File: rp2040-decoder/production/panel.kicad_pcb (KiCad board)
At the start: 4 copper layers, 70 x 70 mm, 535 parts, among them J4 5052702412, Q1 TPM2008, Q2 TPM2008, Q3 TPM2008, Q4 TPM2008, Q5 TPM2008, Q6 TPM2008, Q7 TPM2008, U1 W25Q64JVXGIQ, U2 AP63203WU, U3 RP2040, U4 MD9927, U5 MAX98357A, U6 LMV331, Y1 X252012MMB4SI

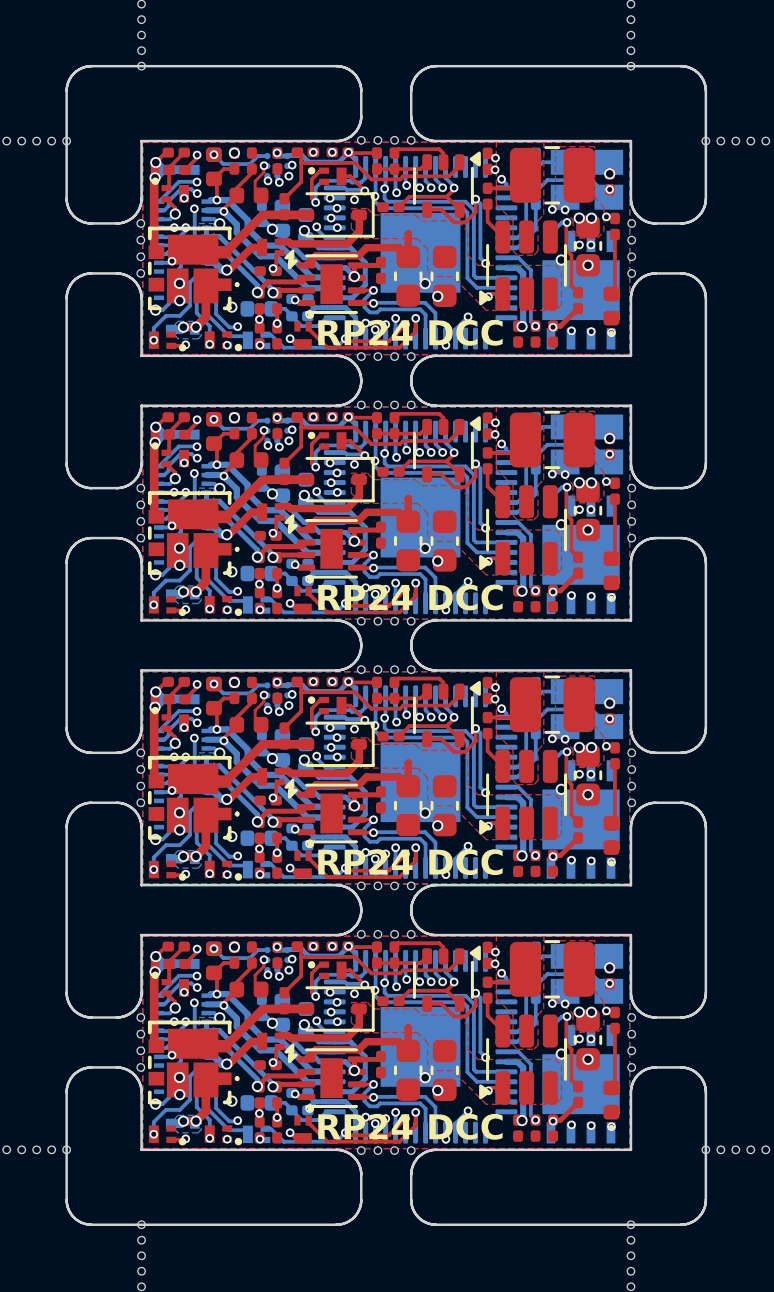
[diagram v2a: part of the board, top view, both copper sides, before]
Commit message: fix: dfm fixes and trace cleanup
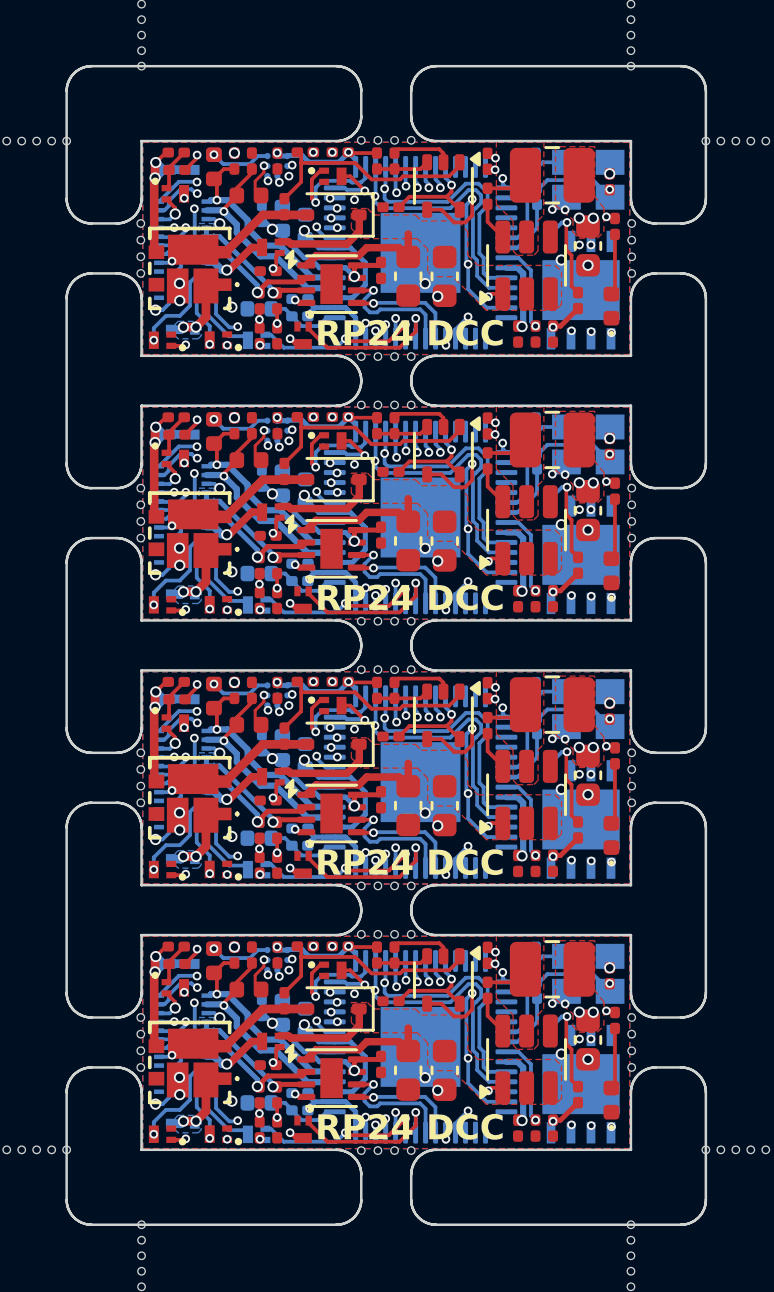
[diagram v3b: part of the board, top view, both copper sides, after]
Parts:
- removed the C8 at (145.3, 38.2)
- removed the C8 at (145.3, 48.8)
- removed the C8 at (145.3, 59.4)
- removed the C8 at (145.3, 70.0)
- removed the R6 at (154.5, 58.2)
- removed the R6 at (154.5, 37.0)
- removed the R6 at (154.5, 47.6)
- removed the R6 at (154.5, 68.8)
- removed the Y1 at (156.5, 36.4)
- removed the Y1 at (156.5, 57.5)
- removed the Y1 at (156.5, 47.0)
- removed the Y1 at (156.5, 68.2)
- added C8: 10uF, Capacitor_SMD:C_0402_1005Metric, B.Cu at (145.3, 38.2)
- added C8: 10uF, Capacitor_SMD:C_0402_1005Metric, B.Cu at (145.3, 70.0)
- added C8: 10uF, Capacitor_SMD:C_0402_1005Metric, B.Cu at (145.3, 48.8)
- added C8: 10uF, Capacitor_SMD:C_0402_1005Metric, B.Cu at (145.3, 59.4)
- added R6: 1K, Resistor_SMD:R_0201_0603Metric, B.Cu at (154.5, 58.2)
- added R6: 1K, Resistor_SMD:R_0201_0603Metric, B.Cu at (154.5, 47.6)
- added R6: 1K, Resistor_SMD:R_0201_0603Metric, B.Cu at (154.5, 68.8)
- added R6: 1K, Resistor_SMD:R_0201_0603Metric, B.Cu at (154.5, 37.0)
- added Y1: X252012MMB4SI, Crystal:Crystal_SMD_2520-4Pin_2.5x2.0mm, B.Cu at (156.6, 47.0)
- added Y1: X252012MMB4SI, Crystal:Crystal_SMD_2520-4Pin_2.5x2.0mm, B.Cu at (156.6, 68.2)
- added Y1: X252012MMB4SI, Crystal:Crystal_SMD_2520-4Pin_2.5x2.0mm, B.Cu at (156.6, 36.4)
- added Y1: X252012MMB4SI, Crystal:Crystal_SMD_2520-4Pin_2.5x2.0mm, B.Cu at (156.6, 57.5)
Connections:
- U3 pad 27: Board_2-unconnected-(U3-GPIO16-Pad27) -> Board_2-/CAP_ENABLE
- U3 pad 27: Board_0-unconnected-(U3-GPIO16-Pad27) -> Board_0-/CAP_ENABLE
- U3 pad 27: Board_1-unconnected-(U3-GPIO16-Pad27) -> Board_1-/CAP_ENABLE
- U3 pad 27: Board_3-unconnected-(U3-GPIO16-Pad27) -> Board_3-/CAP_ENABLE
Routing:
- net Board_1-/CAP_ENABLE: track 15.1 -> 17.2 mm
- net Board_2-/CAP_ENABLE: track 15.1 -> 17.2 mm
- net Board_3-/CAP_ENABLE: track 15.1 -> 17.2 mm
- net Board_0-/CAP_ENABLE: track 15.1 -> 17.2 mm
- net Board_3-/AUX11: track 20.5 -> 21.8 mm
- net Board_1-/AUX11: track 20.5 -> 21.8 mm
- net Board_2-/AUX11: track 20.5 -> 21.8 mm
- net Board_0-/AUX11: track 20.5 -> 21.8 mm
- net Board_3-/AUX12: track 20.1 -> 21.4 mm
- net Board_2-/AUX12: track 20.1 -> 21.4 mm
- net Board_1-/AUX12: track 20.1 -> 21.4 mm
- net Board_0-/AUX12: track 20.1 -> 21.4 mm
- net Board_3-+3.3V: track 43.9 -> 42.6 mm
- net Board_1-+3.3V: track 43.9 -> 42.6 mm
- net Board_2-+3.3V: track 43.9 -> 42.6 mm
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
